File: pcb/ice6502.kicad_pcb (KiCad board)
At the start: 2 copper layers, 100 x 50 mm, 24 parts, among them J1 Programming Header, J2 RDY, J3 RESB, J4 VIN, J5 GND, U0 iCE40-HX4K-TQ144, U1 AT25SF041-SSHD-B, U1_1 W65C816S_PLCC, U2 VXO7803-1000, U3 IS61WV5128EDBLL-10TLI, X1 VC-81

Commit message: learning...
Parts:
- added REF**: MountingHole_3.2mm_M3_Pad, Mounting_Holes:MountingHole_3.2mm_M3_Pad, F.Cu at (146.0, 54.0)
- added REF**: MountingHole_3.2mm_M3_Pad, Mounting_Holes:MountingHole_3.2mm_M3_Pad, F.Cu at (146.0, 96.0)
- added REF**: MountingHole_3.2mm_M3_Pad, Mounting_Holes:MountingHole_3.2mm_M3_Pad, F.Cu at (54.0, 96.0)
- added REF**: MountingHole_3.2mm_M3_Pad, Mounting_Holes:MountingHole_3.2mm_M3_Pad, F.Cu at (54.0, 54.0)
- C1, C2: moved to B.Cu
- U3: moved to F.Cu
- moved U3 33.7 mm to (133.5, 72.4), turned to 180 degrees
- moved J5 10.5 mm to (58.5, 60.5)
- moved J4 10.3 mm to (54.0, 60.5)
- moved J1 5.01 mm to (129.5, 90.2), turned to 270 degrees
- moved U0 1.65 mm to (101.6, 72.4)
- moved C1 0.50 mm to (83.0, 55.5), turned to 90 degrees
- moved C2 0.50 mm to (67.0, 55.5), turned to 270 degrees
- moved C3 0.50 mm to (94.0, 56.5)
- moved C4 0.50 mm to (88.0, 54.5)
- moved U2 0.50 mm to (77.1, 55.4)
- moved VR1 0.50 mm to (91.0, 55.5)
- moved U1_1 0.40 mm to (74.9, 72.4)
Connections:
- net addr_b20 renamed addr_b16
- net addr_b21 renamed addr_b17
- net addr_b22 renamed addr_b18
- LED7 pad 2: N$15 -> N$8
- LED8 pad 2: N$16 (its old number) -> N$15
- U0 pad 41: N$9 -> (no net)
- U0 pad 42: N$10 -> (no net)
- U0 pad 43: N$11 -> (no net)
- U0 pad 44: N$12 -> (no net)
- U0 pad 45: N$13 -> (no net)
- U0 pad 47: N$14 -> (no net)
- U0 pad 48: N$15 -> N$9
- U0 pad 49: N$16 (its old number) -> N$10
- U0 pad 52: (no net) -> N$11
- U0 pad 55: (no net) -> N$12
- U0 pad 56: (no net) -> N$13
- U0 pad 60: (no net) -> N$14
- U0 pad 62: (no net) -> N$15
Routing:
- net N$9: track 0.00 -> 37.1 mm
- net N$6: track 0.00 -> 34.9 mm
- net N$10: track 0.00 -> 34.8 mm
- net N$11: track 0.00 -> 33.4 mm
- net N$12: track 0.00 -> 32.0 mm
- net data0: track 0.00 -> 31.1 mm, vias 0 -> 1
- net N$13: track 0.00 -> 29.7 mm
- net N$2: track 0.00 -> 29.6 mm
- net N$14: track 0.00 -> 28.8 mm
- net N$7: track 0.00 -> 28.5 mm
- net data2: track 0.00 -> 28.4 mm, vias 0 -> 1
- net N$8: track 0.00 -> 26.5 mm
- net data1: track 0.00 -> 26.1 mm, vias 0 -> 1
- net addr_c0: track 0.00 -> 25.2 mm
- net data4: track 0.00 -> 25.1 mm, vias 0 -> 1
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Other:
- rule trace_min: 0.2 -> 0.127
- rule via_min_size: 0.4 -> 0.6

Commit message: wip
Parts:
- added C10: 1uF, C_0805_HandSoldering, B.Cu at (96.1, 79.6)
- added C5: 100nF, C_0805_HandSoldering, B.Cu at (89.5, 95.0)
- added C6: 10nF, C_0805_HandSoldering, B.Cu at (111.0, 91.2)
- added C7: 10uF/50V, C_1210_HandSoldering, F.Cu at (62.2, 53.3)
- added C8: 22uF/10V, C_0805_HandSoldering, F.Cu at (73.0, 59.7)
- added C9: 1uF, C_0805_HandSoldering, B.Cu at (92.9, 76.4)
- added J6: 3v3, Test_Point_Pad_d1.5mm, F.Cu at (108.0, 54.0)
- added J7: 1v2, Test_Point_Pad_d1.5mm, F.Cu at (104.0, 54.0)
- added J8: GND, Test_Point_Pad_d1.5mm, F.Cu at (112.0, 54.0)
- added R1: 10KOhm, R_0805_HandSoldering, F.Cu at (123.3, 77.5)
- added R10: 2.2KOhm, R_0805_HandSoldering, B.Cu at (145.1, 79.0)
- added R11: 2.2KOhm, R_0805_HandSoldering, B.Cu at (145.1, 76.2)
- added R12: 2.2KOhm, R_0805_HandSoldering, B.Cu at (145.1, 73.3)
- added R13: 2.2KOhm, R_0805_HandSoldering, B.Cu at (145.1, 70.5)
- added R14: 2.2KOhm, R_0805_HandSoldering, B.Cu at (145.1, 67.6)
- added R15: 2.2KOhm, R_0805_HandSoldering, B.Cu at (145.1, 64.8)
- added R16: 3.3KOhm, R_0805_HandSoldering, B.Cu at (67.3, 76.0)
- added R17: 2.2KOhm, R_0805_HandSoldering, B.Cu at (67.3, 73.0)
- added R2: 2.2KOhm, R_0805_HandSoldering, F.Cu at (123.1, 81.3)
- added R3: 100Ohm, R_0805_HandSoldering, B.Cu at (101.8, 78.7)
- added R4: 100Ohm, R_0805_HandSoldering, B.Cu at (96.5, 73.3)
- added R5: 10KOhm, R_0805_HandSoldering, F.Cu at (138.3, 86.5)
- added R6: 10KOhm, R_0805_HandSoldering, B.Cu at (91.5, 94.9)
- added R7: 10KOhm, R_0805_HandSoldering, B.Cu at (93.5, 94.9)
- added R8: 2.2KOhm, R_0805_HandSoldering, B.Cu at (145.1, 84.8)
- added R9: 2.2KOhm, R_0805_HandSoldering, B.Cu at (145.1, 81.9)
- C1: value 10uF/50V -> 10uF; footprint C_1210_HandSoldering -> C_0805_HandSoldering
- C2: value 22uF/10V -> 100nF
- C3: value 1uF -> 10uF
- C4: value 1uF -> 100nF
- U1: moved to F.Cu
- VR1: moved to B.Cu
- X1: value VC-81 -> ASE-xxxMHz; footprint Oscillator_DIP-8 -> Oscillator_SMD_Abracon_ASE-4pin_3.2x2.5mm_HandSoldering
- moved LED1 80.6 mm to (145.2, 84.8), turned to 180 degrees
- moved LED2 78.1 mm to (145.2, 81.9), turned to 180 degrees
- moved LED3 75.7 mm to (145.2, 79.0), turned to 180 degrees
- moved LED4 73.4 mm to (145.2, 76.2), turned to 180 degrees
- moved LED5 71.3 mm to (145.2, 73.3), turned to 180 degrees
- moved LED6 69.4 mm to (145.2, 70.5), turned to 180 degrees
- moved LED7 67.7 mm to (145.2, 67.6), turned to 180 degrees
- moved LED8 66.1 mm to (145.2, 64.8), turned to 180 degrees
- moved C2 43.6 mm to (103.1, 79.9), turned to 225 degrees
- moved C1 33.4 mm to (104.4, 81.1), turned to 225 degrees
- moved VR1 21.5 mm to (100.0, 75.0), turned to 45 degrees
- moved C4 19.0 mm to (95.1, 72.1), turned to 225 degrees
- moved U3 15.4 mm to (123.2, 61.0)
- moved C3 14.4 mm to (93.9, 70.9), turned to 225 degrees
- moved J5 9.62 mm to (54.0, 69.0)
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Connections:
- C1 pad 1: VIN -> PLLVCC
- C1 pad 2: N$18 (its old number) -> PLLGND
- C2 pad 1: N$19 -> PLLVCC
- C2 pad 2: N$18 (its old number) -> PLLGND
- C3 pad 1: N$20 (its old number) -> PLLVCC_1
- C3 pad 2: N$21 -> PLLGND_1
- C4 pad 1: N$22 (its old number) -> PLLVCC_1
- C4 pad 2: N$21 -> PLLGND_1
- J1 pad 1: N$5 (its old number) -> 3v3
- J1 pad 2: (no net) -> GND
- J5 pad 1: (no net) -> GND
- LED1 pad 1: (no net) -> N$13
- LED2 pad 1: (no net) -> N$15
- LED3 pad 1: (no net) -> N$17
- LED4 pad 1: (no net) -> N$19
- LED5 pad 1: (no net) -> N$21
- LED6 pad 1: (no net) -> N$23
- LED7 pad 1: (no net) -> N$24
- LED7 pad 2: N$8 -> N$11
- LED8 pad 1: (no net) -> N$26
- U0 pad 1: (no net) -> addr_c11
- U0 pad 10: data4 -> addr_c4
- U0 pad 100: (no net) -> 3v3
- U0 pad 103: (no net) -> GND
- U0 pad 108: (no net) -> 3v3
- U0 pad 11: data5 -> addr_c3
- U0 pad 111: (no net) -> 1v2
- U0 pad 12: data6 -> addr_c2
- U0 pad 123: (no net) -> 3v3
- U0 pad 126: (no net) -> PLLVCC_1
- U0 pad 127: (no net) -> PLLGND_1
- U0 pad 129: (no net) -> data_c0
- U0 pad 13: (no net) -> GND
- U0 pad 130: (no net) -> data_c1
- U0 pad 131: (no net) -> 3v3
- U0 pad 132: (no net) -> GND
- U0 pad 134: (no net) -> data_c2
- U0 pad 135: (no net) -> data_c3
- U0 pad 136: (no net) -> data_c4
- U0 pad 137: (no net) -> data_c5
- U0 pad 138: (no net) -> data_c6
- U0 pad 139: (no net) -> data_c7
- U0 pad 14: (no net) -> GND
- U0 pad 140: (no net) -> GND
- U0 pad 141: (no net) -> addr_c15
- U0 pad 142: (no net) -> addr_c14
- U0 pad 143: (no net) -> addr_c13
- U0 pad 144: (no net) -> addr_c12
- U0 pad 15: data7 -> addr_c1
- U0 pad 16: (no net) -> addr_c0
- U0 pad 17: addr_c15 -> (no net)
- U0 pad 18: addr_c14 -> (no net)
- U0 pad 19: addr_c13 -> (no net)
- U0 pad 2: (no net) -> addr_c10
- U0 pad 20: addr_c12 -> (no net)
- U0 pad 21: addr_c11 -> (no net)
- U0 pad 22: addr_c10 -> (no net)
- U0 pad 23: addr_c9 -> (no net)
- U0 pad 24: addr_c8 -> (no net)
- U0 pad 25: addr_c7 -> (no net)
- U0 pad 26: addr_c6 -> (no net)
- U0 pad 27: (no net) -> 1v2
- U0 pad 28: addr_c5 -> (no net)
- U0 pad 29: addr_c4 -> (no net)
- U0 pad 3: (no net) -> addr_c9
- U0 pad 30: (no net) -> 3v3
- U0 pad 31: addr_c3 -> (no net)
- U0 pad 32: addr_c2 -> (no net)
- U0 pad 33: addr_c1 -> (no net)
- U0 pad 34: addr_c0 -> (no net)
- U0 pad 4: data0 -> addr_c8
- U0 pad 40: (no net) -> 1v2
- U0 pad 46: (no net) -> 3v3
- U0 pad 5: (no net) -> GND
- U0 pad 53: (no net) -> PLLGND
- U0 pad 54: (no net) -> PLLVCC
- U0 pad 57: (no net) -> 3v3
- U0 pad 59: (no net) -> GND
- U0 pad 6: (no net) -> 3v3
- U0 pad 61: N$8 -> N$11
- U0 pad 69: (no net) -> GND
- U0 pad 7: data1 -> addr_c7
- U0 pad 72: N$5 (its old number) -> 3v3
- U0 pad 8: data2 -> addr_c6
- U0 pad 86: (no net) -> GND
- U0 pad 89: (no net) -> 3v3
- U0 pad 9: data3 -> addr_c5
- U0 pad 92: (no net) -> 1v2
- U1 pad 3: (no net) -> N$9
- U1 pad 4: (no net) -> GND
- U1 pad 7: (no net) -> N$10
- U1 pad 8: N$5 (its old number) -> 3v3
- U1_1 pad 1: (no net) -> GND
- U1_1 pad 23: (no net) -> GND
- U1_1 pad 24: (no net) -> GND
- U1_1 pad 29: data7 -> data_c7
- U1_1 pad 30: data6 -> data_c6
- U1_1 pad 31: data5 -> data_c5
- U1_1 pad 32: data4 -> data_c4
- U1_1 pad 33: data3 -> data_c3
- U1_1 pad 34: data2 -> data_c2
- U1_1 pad 35: data1 -> data_c1
- U1_1 pad 36: data0 -> data_c0
- U1_1 pad 37: (no net) -> 3v3
- U1_1 pad 9: (no net) -> 3v3
- U2 pad 2: N$18 (its old number) -> GND
- U2 pad 3: N$19 -> 3v3
- U3 pad 10: data1 -> (no net)
- U3 pad 11: (no net) -> 3v3
- U3 pad 12: (no net) -> GND
- U3 pad 13: data2 -> (no net)
- U3 pad 14: data3 -> (no net)
- U3 pad 31: data4 -> (no net)
- U3 pad 32: data5 -> (no net)
- U3 pad 33: (no net) -> 3v3
- U3 pad 34: (no net) -> GND
- U3 pad 35: data6 -> (no net)
- U3 pad 36: data7 -> (no net)
- U3 pad 9: data0 -> (no net)
- VR1 pad 1: N$22 (its old number) -> 1v2
- VR1 pad 2: N$21 -> GND
- VR1 pad 3: N$21 -> GND
- VR1 pad 4: N$20 (its old number) -> 3v3
- VR1 pad 5: N$20 (its old number) -> 3v3
- VR1 pad 6: N$21 -> GND
- VR1 pad 7: N$21 -> GND
- X1 pad 1: (no net) -> 3v3
- X1 pad 4: (no net) -> 3v3
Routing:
- net 1v2: track 0.00 -> 49.7 mm, vias 0 -> 2
- net N$12: track 37.1 -> 0.00 mm
- net N$3: track 34.9 -> 0.00 mm
- net N$14: track 34.8 -> 0.00 mm
- net N$16: track 33.4 -> 0.00 mm
- net N$18: track 32.0 -> 0.00 mm
- net data_c0: track 0.00 -> 31.4 mm
- net data0: track 31.1 -> 0.00 mm, vias 1 -> 0
- net N$20: track 29.7 -> 0.00 mm
- net N$5: track 29.6 -> 0.00 mm
- net N$22: track 28.8 -> 0.00 mm
- net N$2: track 28.5 -> 0.00 mm
- net data2: track 28.4 -> 0.00 mm, vias 1 -> 0
- net data_c2: track 0.00 -> 27.3 mm
- net N$8: track 26.5 -> 0.00 mm
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
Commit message: Playing with pcbnew
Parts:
- C7, C8, J6, J7, J8: moved to B.Cu
- R16, R17: moved to F.Cu
- moved R5 21.7 mm to (117.7, 80.0), turned to 180 degrees
- moved R3 14.3 mm to (110.4, 90.2), turned to 0 degrees
- moved R4 12.2 mm to (93.3, 61.5), turned to 270 degrees
- moved R17 11.9 mm to (55.6, 71.0), turned to 0 degrees
- moved R16 11.7 mm to (55.6, 77.0), turned to 0 degrees
- moved C9 11.2 mm to (102.6, 70.9), turned to 315 degrees
- moved C2 11.2 mm to (110.5, 88.3), turned to 180 degrees
- moved C4 11.1 mm to (91.4, 61.6), turned to 90 degrees
- moved C3 10.2 mm to (89.5, 61.6), turned to 90 degrees
- moved U2 9.24 mm to (68.0, 54.0), turned to 270 degrees
- moved C1 8.06 mm to (110.5, 86.4), turned to 180 degrees
- moved R1 7.22 mm to (117.7, 82.0), turned to 180 degrees
- moved R2 6.10 mm to (117.7, 84.0), turned to 180 degrees
- moved C6 5.90 mm to (107.5, 95.9)
- moved X1 5.90 mm to (107.5, 95.9)
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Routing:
- net 3v3: track 19.2 -> 210.1 mm, vias 2 -> 16
- net GND: track 8.30 -> 29.9 mm, vias 2 -> 11
- net 1v2: track 49.7 -> 66.6 mm, vias 2 -> 4
- net VIN: track 0.00 -> 16.3 mm
- net PLLGND_1: track 6.27 -> 16.8 mm
- net N$27: track 2.46 -> 10.7 mm
- net N$3: track 0.00 -> 7.43 mm
- net PLLVCC: track 6.79 -> 14.0 mm
- net PLLVCC_1: track 7.10 -> 14.0 mm
- net N$2: track 0.00 -> 6.27 mm
- net PLLGND: track 5.61 -> 10.4 mm
- net N$7: track 0.00 -> 4.68 mm
- net N$28: track 5.70 -> 7.87 mm
- added copper zone on B.Cu, net GND
- added copper zone on F.Cu, net GND

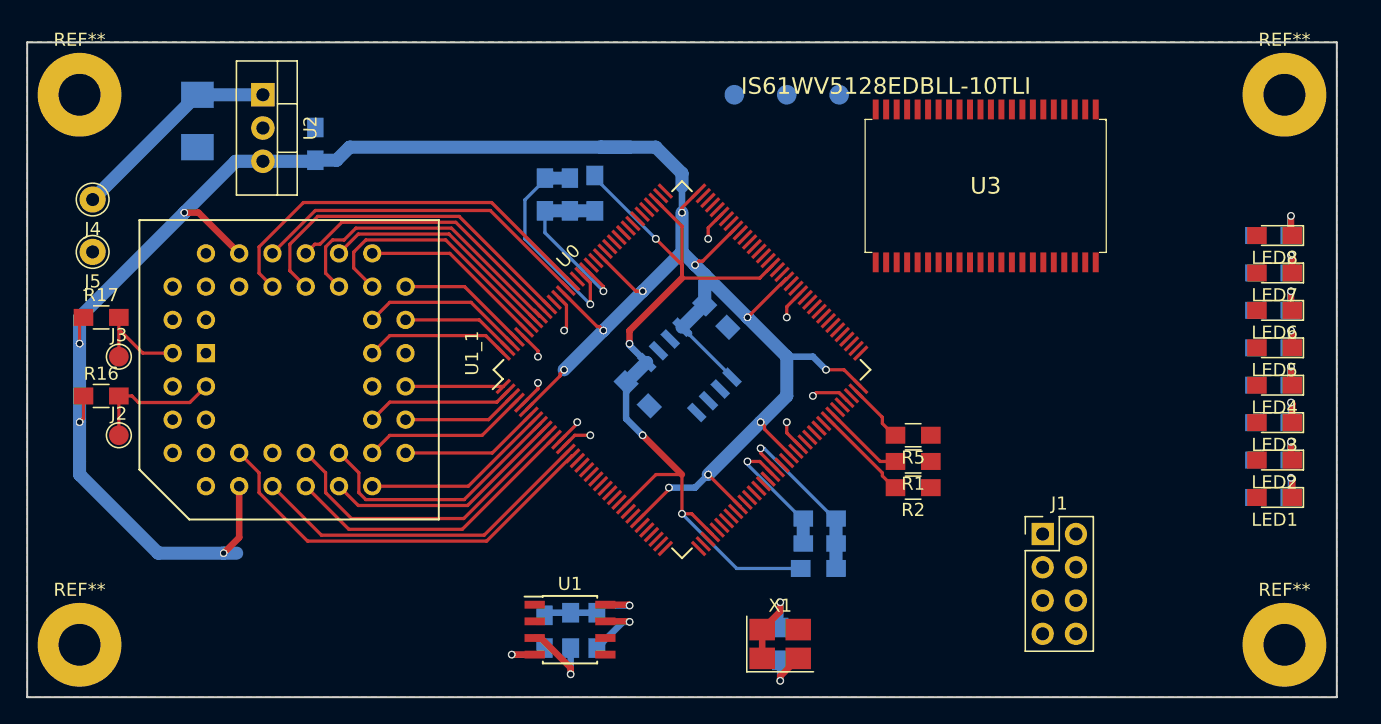
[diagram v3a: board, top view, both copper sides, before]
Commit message: Cleanup led & 3v3 pour on top layer
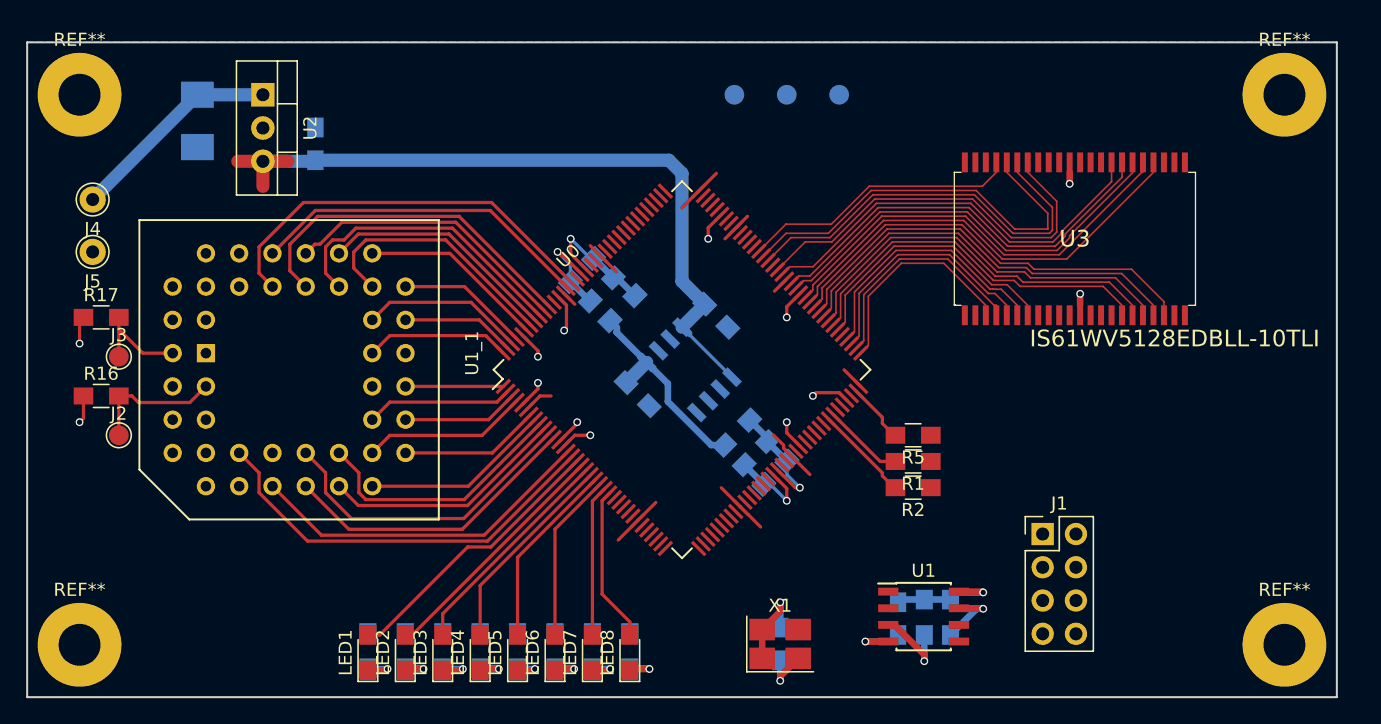
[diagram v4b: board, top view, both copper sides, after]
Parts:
- moved LED1 70.2 mm to (76.0, 96.6), turned to 90 degrees
- moved R8 70.1 mm to (76.0, 96.4), turned to 90 degrees
- moved LED2 68.0 mm to (78.9, 96.6), turned to 90 degrees
- moved R9 67.8 mm to (78.9, 96.4), turned to 90 degrees
- moved LED3 65.9 mm to (81.7, 96.6), turned to 90 degrees
- moved R10 65.7 mm to (81.7, 96.4), turned to 90 degrees
- moved LED4 64.0 mm to (84.6, 96.6), turned to 90 degrees
- moved R11 63.8 mm to (84.6, 96.4), turned to 90 degrees
- moved LED5 62.3 mm to (87.4, 96.6), turned to 90 degrees
- moved R12 62.1 mm to (87.4, 96.4), turned to 90 degrees
- moved LED6 60.8 mm to (90.3, 96.6), turned to 90 degrees
- moved R13 60.6 mm to (90.3, 96.4), turned to 90 degrees
- moved LED7 59.6 mm to (93.2, 96.6), turned to 90 degrees
- moved R14 59.4 mm to (93.2, 96.4), turned to 90 degrees
- moved LED8 58.6 mm to (96.0, 96.6), turned to 90 degrees
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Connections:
- LED7 pad 2: N$11 -> N$24
- LED8 pad 2: N$25 (its old number) -> N$26
- U0 pad 101: addr_b5 -> data4
- U0 pad 102: addr_b4 -> data5
- U0 pad 104: addr_b3 -> data6
- U0 pad 105: addr_b2 -> data7
- U0 pad 106: addr_b1 -> (no net)
- U0 pad 107: addr_b0 -> (no net)
- U0 pad 17: (no net) -> N$12
- U0 pad 18: (no net) -> N$14
- U0 pad 19: (no net) -> N$16
- U0 pad 20: (no net) -> N$18
- U0 pad 21: (no net) -> N$20
- U0 pad 22: (no net) -> N$22
- U0 pad 23: (no net) -> N$24
- U0 pad 24: (no net) -> N$26
- U0 pad 48: N$12 -> (no net)
- U0 pad 49: N$14 -> (no net)
- U0 pad 52: N$16 -> (no net)
- U0 pad 55: N$18 -> (no net)
- U0 pad 56: N$20 -> (no net)
- U0 pad 60: N$22 -> (no net)
- U0 pad 62: N$25 (its old number) -> (no net)
- U0 pad 73: (no net) -> addr_b0
- U0 pad 74: (no net) -> addr_b1
- U0 pad 75: (no net) -> addr_b2
- U0 pad 76: (no net) -> addr_b3
- U0 pad 78: (no net) -> addr_b4
- U0 pad 79: (no net) -> addr_b5
- U0 pad 80: (no net) -> addr_b6
- U0 pad 81: (no net) -> addr_b7
- U0 pad 82: (no net) -> addr_b8
- U0 pad 83: (no net) -> addr_b9
- U0 pad 84: addr_b18 -> addr_b10
- U0 pad 85: addr_b17 -> addr_b11
- U0 pad 87: addr_b16 -> addr_b12
- U0 pad 88: addr_b15 -> addr_b13
- U0 pad 91: addr_b13 -> addr_b15
- U0 pad 93: addr_b12 -> addr_b16
- U0 pad 94: addr_b11 -> addr_b17
- U0 pad 95: addr_b10 -> addr_b18
- U0 pad 96: addr_b9 -> data0
- U0 pad 97: addr_b8 -> data1
- U0 pad 98: addr_b7 -> data2
- U0 pad 99: addr_b6 -> data3
- U3 pad 10: (no net) -> data1
- U3 pad 13: (no net) -> data2
- U3 pad 14: (no net) -> data3
- U3 pad 31: (no net) -> data4
- U3 pad 32: (no net) -> data5
- U3 pad 35: (no net) -> data6
- U3 pad 36: (no net) -> data7
- U3 pad 9: (no net) -> data0
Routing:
- net 3v3: track 210.1 -> 105.4 mm, vias 16 -> 4
- net 1v2: track 66.6 -> 16.3 mm, vias 4 -> 0
- net addr_b10: track 0.00 -> 33.1 mm
- net addr_b9: track 0.00 -> 32.5 mm
- net addr_b11: track 0.00 -> 32.4 mm
- net addr_b12: track 0.00 -> 31.9 mm
- net addr_b13: track 0.00 -> 31.5 mm
- net addr_b14: track 0.00 -> 31.3 mm
- net addr_b8: track 0.00 -> 31.2 mm
- net addr_b16: track 0.00 -> 30.6 mm
- net addr_b17: track 0.00 -> 30.6 mm
- net addr_b15: track 0.00 -> 30.4 mm
- net addr_b7: track 0.00 -> 30.1 mm
- net addr_b6: track 0.00 -> 28.9 mm
- net addr_b5: track 0.00 -> 27.8 mm
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- added copper zone on F.Cu, net 3v3
- removed copper zone on F.Cu, net GND

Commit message: Cleanup pcb & start naming nets
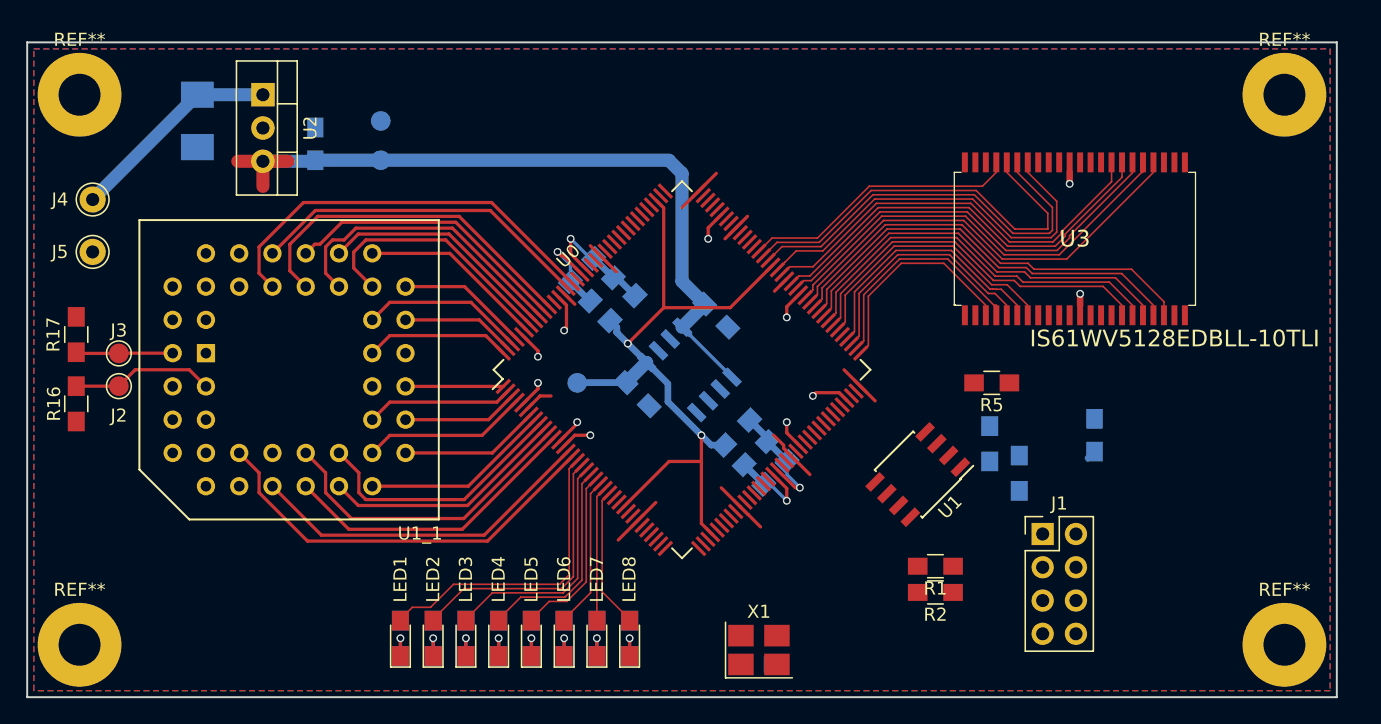
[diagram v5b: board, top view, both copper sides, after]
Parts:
- moved J8 35.1 mm to (77.0, 56.0)
- moved J6 31.4 mm to (77.0, 59.0)
- moved J7 25.1 mm to (92.0, 76.0)
- moved C5 20.5 mm to (131.5, 80.0)
- moved R6 14.2 mm to (123.5, 80.7)
- moved R7 12.2 mm to (125.8, 82.9)
- moved U1 10.9 mm to (118.0, 83.0), turned to 225 degrees
- moved R1 8.18 mm to (119.3, 90.0)
- moved R2 8.18 mm to (119.3, 92.0)
- moved R5 7.21 mm to (123.7, 76.0)
- moved J2 3.75 mm to (57.0, 76.2)
- moved LED1 2.72 mm to (78.5, 95.5)
- moved R8 2.66 mm to (78.5, 95.5)
- moved LED2 2.39 mm to (81.0, 95.5)
- moved C6 2.35 mm to (105.8, 97.5), turned to 0 degrees
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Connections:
- net N$4 renamed SCK
- net N$5 renamed MOSI
- net N$6 renamed MISO
- net N$7 renamed CS
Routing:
- net 1v2: track 16.3 -> 57.4 mm, vias 0 -> 2
- net 3v3: track 105.4 -> 87.5 mm, vias 4 -> 0
- net GND: track 31.7 -> 24.1 mm, vias 13 -> 11
- net N$3: track 7.43 -> 0.00 mm
- net N$2: track 6.27 -> 0.00 mm
- net N$9: track 6.19 -> 0.00 mm, vias 1 -> 0
- net N$10: track 5.19 -> 0.00 mm, vias 1 -> 0
- net CS: track 4.68 -> 0.00 mm
- net N$14: track 18.9 -> 20.9 mm
- net N$12: track 21.5 -> 23.4 mm
- net N$22: track 13.0 -> 11.6 mm
- net N$16: track 17.2 -> 18.5 mm
- net N$24: track 11.6 -> 10.4 mm
- net N$26: track 12.0 -> 10.9 mm
- net N$20: track 14.4 -> 13.6 mm
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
